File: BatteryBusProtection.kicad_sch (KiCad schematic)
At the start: 10 parts, among them U4 SIRA99DP-T1-GE3, U5 SIRA99DP-T1-GE3, U6 SIRA99DP-T1-GE3, U7 SIRA99DP-T1-GE3, U8 LTC4412xS6, U9 LTC4412xS6

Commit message: First pass at new schematics and board
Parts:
- added F2, F3: 6A, Fuse:Fuse_0805_2012Metric, symbol Device:Polyfuse
- U4, U5, U6, U7: footprint MOSFET_7DP-T1-GE3_VIS -> Battery-Board:MOSFET_7DP-T1-GE3_VIS
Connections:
- net BATT2: now also F2.1, F3.2; no longer U4.1 (S), U4.2 (S), U4.3 (S), U6.5 (D), U6.6 (D), U6.7 (D), U6.8 (D)
- net at R13.1: now also U4.1 (S), U4.2 (S), U4.3 (S), F3.1
- net CHARGE_ENABLE renamed CHARGE_EN
- net DISCHARGE_ENABLE renamed DISCHARGE_EN
- new net: F2.2, U6.5 (D), U6.6 (D), U6.7 (D), U6.8 (D)
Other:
- moved on the sheet: R13

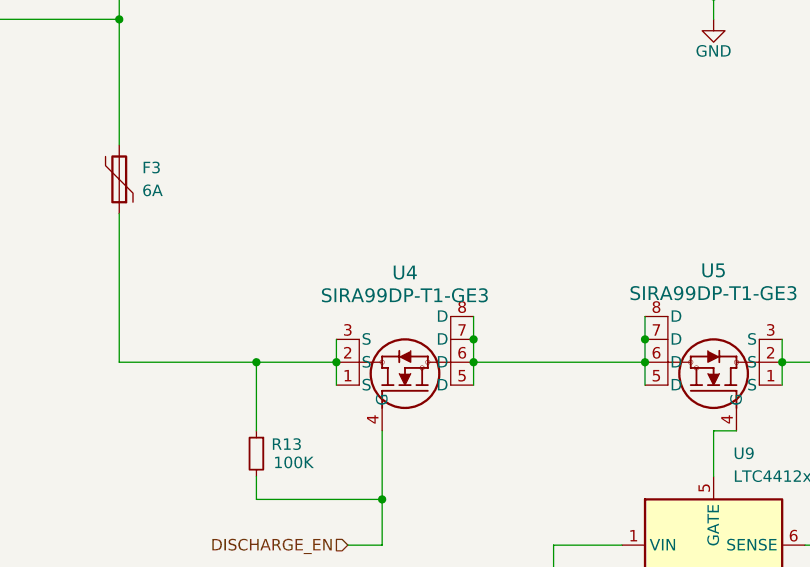
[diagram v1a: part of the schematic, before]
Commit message: Changes for lib refactor
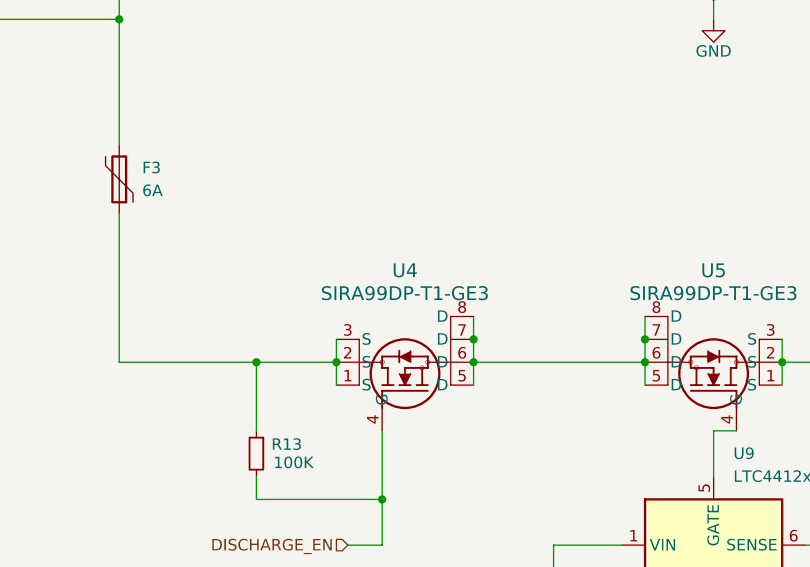
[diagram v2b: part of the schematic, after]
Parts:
- U4, U5, U6, U7: footprint Battery-Board:MOSFET_7DP-T1-GE3_VIS -> Argus-Misc:MOSFET_7DP-T1-GE3_VIS; symbol Battery-Board:SIRA99DP-T1-GE3 -> Argus-Misc:SIRA99DP-T1-GE3
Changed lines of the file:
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@@
 	)
 	(symbol
-		(lib_id "Battery-Board:SIRA99DP-T1-GE3")
+		(lib_id "Argus-Misc:SIRA99DP-T1-GE3")
 		(at 85.09 92.71 270)
 		(mirror x)
@@
 			)
 		)
-		(property "Footprint" "Battery-Board:MOSFET_7DP-T1-GE3_VIS"
+		(property "Footprint" "Argus-Misc:MOSFET_7DP-T1-GE3_VIS"
 			(at 85.09 92.71 0)
 			(effects
@@
 	)
 	(symbol
-		(lib_id "Battery-Board:SIRA99DP-T1-GE3")
+		(lib_id "Argus-Misc:SIRA99DP-T1-GE3")
 		(at 114.3 92.71 90)
 		(unit 1)
@@
 			)
 		)
-		(property "Footprint" "Battery-Board:MOSFET_7DP-T1-GE3_VIS"
+		(property "Footprint" "Argus-Misc:MOSFET_7DP-T1-GE3_VIS"
 			(at 114.3 92.71 0)
 			(effects
@@
 	)
 	(symbol
-		(lib_id "Battery-Board:SIRA99DP-T1-GE3")
+		(lib_id "Argus-Misc:SIRA99DP-T1-GE3")
 		(at 119.38 168.91 270)
 		(mirror x)
@@
 			)
 		)
-		(property "Footprint" "Battery-Board:MOSFET_7DP-T1-GE3_VIS"
+		(property "Footprint" "Argus-Misc:MOSFET_7DP-T1-GE3_VIS"
 			(at 119.38 168.91 0)
 			(effects
@@
 	)
 	(symbol
-		(lib_id "Battery-Board:SIRA99DP-T1-GE3")
+		(lib_id "Argus-Misc:SIRA99DP-T1-GE3")
 		(at 80.01 168.91 90)
 		(unit 1)
@@
 		(fields_autoplaced yes)
 		(property "Reference" "U4"
-			(at 82.55 151.3682 90)
+			(at 82.55 151.13 90)
 			(effects
 				(font
@@
 		)
 		(property "Value" "SIRA99DP-T1-GE3"
-			(at 82.55 153.9082 90)
+			(at 82.55 153.67 90)
 			(effects
 				(font
@@
 			)
 		)
-		(property "Footprint" "Battery-Board:MOSFET_7DP-T1-GE3_VIS"
+		(property "Footprint" "Argus-Misc:MOSFET_7DP-T1-GE3_VIS"
 			(at 80.01 168.91 0)
 			(effects

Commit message: Fixes from feedback
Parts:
- U4, U5, U6, U7: footprint Argus-Misc:MOSFET_7DP-T1-GE3_VIS -> MOSFET_7DP-T1-GE3_VIS
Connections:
- net SYSTEM_VDD: now also C10.1, U8.1 (VIN)
- net at C11.1, U9.1 (VIN): now also U4.5 (D), U4.6 (D), U4.7 (D), U4.8 (D), U5.5 (D), U5.6 (D), U5.7 (D), U5.8 (D)
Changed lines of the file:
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@@
+	)
+	(junction
+		(at 99.06 161.29)
+		(diameter 0)
+		(color 0 0 0 0)
 	)
 	(junction
@@
 	)
 	(junction
+		(at 134.62 85.09)
+		(diameter 0)
+		(color 0 0 0 0)
+	)
+	(junction
 		(at 109.22 85.09)
 		(diameter 0)
@@
 	)
 	(junction
+		(at 99.06 181.61)
+		(diameter 0)
+		(color 0 0 0 0)
+	)
+	(junction
 		(at 109.22 158.75)
 		(diameter 0)
@@
 	)
 	(junction
+		(at 134.62 105.41)
+		(diameter 0)
+		(color 0 0 0 0)
+	)
+	(junction
 		(at 116.84 120.65)
 		(diameter 0)
@@
 	(wire
 		(pts
-			(xy 152.4 85.09) (xy 124.46 85.09)
+			(xy 152.4 85.09) (xy 134.62 85.09)
 		)
 		(stroke
@@
 	(wire
 		(pts
+			(xy 134.62 85.09) (xy 134.62 105.41)
+		)
+		(stroke
+			(width 0)
+			(type default)
+		)
+	)
+	(wire
+		(pts
 			(xy 74.93 85.09) (xy 74.93 87.63)
 		)
@@
 	(wire
 		(pts
+			(xy 99.06 161.29) (xy 99.06 181.61)
+		)
+		(stroke
+			(width 0)
+			(type default)
+		)
+	)
+	(wire
+		(pts
 			(xy 116.84 92.71) (xy 114.3 92.71)
 		)
@@
 	(wire
 		(pts
-			(xy 90.17 161.29) (xy 109.22 161.29)
+			(xy 90.17 161.29) (xy 99.06 161.29)
 		)
 		(stroke
@@
 	(wire
 		(pts
+			(xy 134.62 85.09) (xy 124.46 85.09)
+		)
+		(stroke
+			(width 0)
+			(type default)
+		)
+	)
+	(wire
+		(pts
 			(xy 76.2 105.41) (xy 85.09 105.41)
 		)
@@
 		(pts
 			(xy 90.17 161.29) (xy 90.17 163.83)
+		)
+		(stroke
+			(width 0)
+			(type default)
+		)
+	)
+	(wire
+		(pts
+			(xy 99.06 161.29) (xy 109.22 161.29)
 		)
 		(stroke
@@
 			)
 		)
-		(property "Footprint" "Argus-Misc:MOSFET_7DP-T1-GE3_VIS"
+		(property "Footprint" "MOSFET_7DP-T1-GE3_VIS"
 			(at 85.09 92.71 0)
 			(effects
@@
 			)
 		)
-		(property "Footprint" "Argus-Misc:MOSFET_7DP-T1-GE3_VIS"
+		(property "Footprint" "MOSFET_7DP-T1-GE3_VIS"
 			(at 114.3 92.71 0)
 			(effects
@@
 			)
 		)
-		(property "Footprint" "Argus-Misc:MOSFET_7DP-T1-GE3_VIS"
+		(property "Footprint" "MOSFET_7DP-T1-GE3_VIS"
 			(at 119.38 168.91 0)
 			(effects
@@
 			)
 		)
-		(property "Footprint" "Argus-Misc:MOSFET_7DP-T1-GE3_VIS"
+		(property "Footprint" "MOSFET_7DP-T1-GE3_VIS"
 			(at 80.01 168.91 0)
 			(effects

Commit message: v2.1 (v3?) Partial Updates
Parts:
- removed U4, U5, U6, U7: SIRA99DP-T1-GE3, MOSFET_7DP-T1-GE3_VIS, symbol Argus-Misc:SIRA99DP-T1-GE3
- added Q11, Q12, Q13, Q14: SIRA99DP-T1-GE3, Package_SO:PowerPAK_SO-8_Single, symbol Transistor_FET:Si7141DP
- added R44, R47: 470k, Resistor_SMD:R_0603_1608Metric, symbol Device:R_Small
- F7: renamed from F2; footprint Fuse:Fuse_0805_2012Metric -> Fuse:Fuse_1206_3216Metric
- F8: renamed from F3; footprint Fuse:Fuse_0805_2012Metric -> Fuse:Fuse_1206_3216Metric
- R45: renamed from R12; value 100K -> 100k
- R46: renamed from R13; value 100K -> 100k
- renumbered C10 to C7, C11 to C8, U8 to U4, U9 to U5
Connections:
- net CHARGE_ACTIVE: now also R44.2
- net CHARGE_EN: now also Q11.4 (G)
- net DISCHARGE_ACTIVE: now also R47.2
- net DISCHARGE_EN: now also Q13.4 (G)
- net SYSTEM_VDD: now also Q12.5 (D), Q14.1 (S), Q14.2 (S), Q14.3 (S)
- net at F8.1, R46.1: now also Q13.1 (S), Q13.2 (S), Q13.3 (S)
- net at R45.1, U4.6 (SENSE): now also Q11.1 (S), Q11.2 (S), Q11.3 (S), Q12.1 (S), Q12.2 (S), Q12.3 (S)
- net at F7.2: now also Q11.5 (D)
- net at U4.5 (GATE): now also Q12.4 (G)
- net at C8.1, U5.1 (VIN): now also Q13.5 (D), Q14.5 (D)
- net at U5.5 (GATE): now also Q14.4 (G)
- net BATT2 renamed BATT_P
- net GND renamed SYSTEM_VSS
- new net +3V3: R44.1, R47.1
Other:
- note added: "(A bit pointless to have this)"
- note added: "Battery protection design derived from Portland State University's Open-Source OreSat project"
- note added: "CHARGE SWITCH"
- note added: "DISCHARGE SWITCH"
- company: (none) -> Carnegie Mellon University
- title: (none) -> Argus Batteryboard
- moved on the sheet: C7, C8, F7, F8, R45, R46, U4, U5

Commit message: Finalized updates with recommendations and exported files
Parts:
- F7, F8: symbol Device:Polyfuse -> Device:Fuse; Flight (none) -> 0R
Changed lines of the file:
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@@
 		(shape bidirectional)
 		(at 90.17 45.72 180)
-		(fields_autoplaced yes)
 		(effects
 			(font
@@
 		(shape output)
 		(at 198.12 135.89 0)
-		(fields_autoplaced yes)
 		(effects
 			(font
@@
 		(shape output)
 		(at 116.84 71.12 180)
-		(fields_autoplaced yes)
 		(effects
 			(font
@@
 		(shape input)
 		(at 119.38 130.81 180)
-		(fields_autoplaced yes)
 		(effects
 			(font
@@
 		(shape input)
 		(at 133.35 66.04 180)
-		(fields_autoplaced yes)
 		(effects
 			(font
@@
 	)
 	(symbol
-		(lib_id "Device:Polyfuse")
+		(lib_id "Device:Fuse")
 		(at 113.03 110.49 270)
 		(unit 1)
@@
 		(dnp no)
 		(property "Reference" "F8"
-			(at 113.03 105.664 90)
+			(at 113.03 106.172 90)
 			(effects
 				(font
@@
 		)
 		(property "Value" "6A"
-			(at 113.03 107.696 90)
+			(at 113.03 108.204 90)
 			(effects
 				(font
@@
 		)
 		(property "Footprint" "Fuse:Fuse_1206_3216Metric"
-			(at 107.95 111.76 0)
-			(effects
-				(font
-					(size 1.27 1.27)
-				)
-				(justify left)
+			(at 113.03 108.712 90)
+			(effects
+				(font
+					(size 1.27 1.27)
+				)
 				(hide yes)
 			)
@@
 			)
 		)
-		(property "Description" "Resettable fuse, polymeric positive temperature coefficient"
+		(property "Description" "Fuse"
 			(at 113.03 110.49 0)
 			(effects
@@
 				)
 				(hide yes)
+			)
+		)
+		(property "Flight" "0R"
+			(at 113.03 112.776 90)
+			(effects
+				(font
+					(size 1.27 1.27)
+				)
 			)
 		)
@@
 	)
 	(symbol
-		(lib_id "Device:Polyfuse")
+		(lib_id "Device:Fuse")
 		(at 113.03 45.72 90)
 		(unit 1)
@@
 		(dnp no)
 		(property "Reference" "F7"
-			(at 113.03 41.148 90)
+			(at 113.03 41.402 90)
 			(effects
 				(font
@@
 		)
 		(property "Value" "6A"
-			(at 113.03 43.18 90)
+			(at 113.03 43.434 90)
 			(effects
 				(font
@@
 		)
 		(property "Footprint" "Fuse:Fuse_1206_3216Metric"
-			(at 118.11 44.45 0)
-			(effects
-				(font
-					(size 1.27 1.27)
-				)
-				(justify left)
+			(at 113.03 47.498 90)
+			(effects
+				(font
+					(size 1.27 1.27)
+				)
 				(hide yes)
 			)
@@
 			)
 		)
-		(property "Description" "Resettable fuse, polymeric positive temperature coefficient"
+		(property "Description" "Fuse"
 			(at 113.03 45.72 0)
 			(effects
@@
 			)
 		)
+		(property "Flight" "0R"
+			(at 113.03 47.752 90)
+			(effects
+				(font
+					(size 1.27 1.27)
+				)
+			)
+		)
